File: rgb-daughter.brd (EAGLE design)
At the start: 226.1 x 74 mm, 11 parts, among them J1 INPUT

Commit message: feat(planck): add caps
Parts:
- added C10, C11, C12, C13, C15, C16, C17, C18, C19, C2, C20, C21, C22, C23, C24, C25, C26, C27, C28, C29, C3, C30, C31, C32, C33, C34, C35, C36, C37, C38, C39, C4, C40, C41, C42, C43, C44, C45, C46, C47, C48, C5, C6, C7, C8, C9: 0.1uF, SparkFun-Capacitors:0603
- added FRAME2: FRAME-LETTER, SparkFun-Aesthetics:CREATIVE_COMMONS
- added LED10, LED11, LED12, LED13, LED14, LED15, LED16, LED17, LED18, LED19, LED20, LED21, LED22, LED23, LED24, LED25, LED26, LED27, LED28, LED29, LED30, LED31, LED32, LED33, LED34, LED35, LED36, LED37, LED38, LED39, LED40, LED41, LED42, LED43, LED44, LED45, LED46, LED47, LED7, LED8, LED9: WS2812B5050, adafruit:WS2812B
- C1: value 100uF -> 0.1uF; device capacitor-wima:C2.5-3 -> SparkFun-Capacitors:0603
- J1: device SparkFun-Connectors:1X05 -> SparkFun-Connectors:1X05_1.27MM
- moved LED6 10.3 mm to (113.2, 3.17)
- moved C1 5.24 mm to (22.9, -10.2)
- moved R1 3.81 mm to (36.8, 35.6)
- moved J1 3.39 mm to (39.1, 47.2)
- moved LED3 0.99 mm to (46.5, 3.17)
- moved LED4 0.99 mm to (65.5, 3.17)
- moved LED5 0.99 mm to (84.6, 3.17)
- moved LED2 0.99 mm to (27.4, 3.17)
- moved LED1 0.13 mm to (8.37, 3.17)
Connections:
- new net DO: LED23.2-DOUT, LED25.4-DIN
- new net N$10: LED8.2-DOUT, LED9.4-DIN
- new net N$11: LED10.4-DIN, LED9.2-DOUT
- new net N$12: LED10.2-DOUT, LED11.4-DIN
- new net N$13: LED11.2-DOUT, LED12.4-DIN
- new net N$14: LED14.2-DOUT, LED15.4-DIN
- new net N$15: LED15.2-DOUT, LED16.4-DIN
- new net N$16: LED16.2-DOUT, LED17.4-DIN
- new net N$17: LED17.2-DOUT, LED18.4-DIN
- new net N$18: LED19.2-DOUT, LED20.4-DIN
- new net N$19: LED20.2-DOUT, LED21.4-DIN
- new net N$20: LED21.2-DOUT, LED22.4-DIN
- new net N$21: LED22.2-DOUT, LED23.4-DIN
- new net N$22: LED24.4-DIN, LED47.2-DOUT
- new net N$23: LED6.2-DOUT, LED7.4-DIN
- new net N$24: LED13.2-DOUT, LED14.4-DIN
- new net N$25: LED18.2-DOUT, LED19.4-DIN
- new net N$26: LED25.2-DOUT, LED26.4-DIN
- new net N$29: LED26.2-DOUT, LED27.4-DIN
- new net N$30: LED27.2-DOUT, LED28.4-DIN
- new net N$31: LED28.2-DOUT, LED29.4-DIN
- new net N$32: LED29.2-DOUT, LED30.4-DIN
- new net N$33: LED31.2-DOUT, LED32.4-DIN
- new net N$34: LED32.2-DOUT, LED33.4-DIN
- new net N$35: LED33.2-DOUT, LED34.4-DIN
- new net N$36: LED34.2-DOUT, LED35.4-DIN
- new net N$37: LED35.2-DOUT, LED36.4-DIN
- new net N$38: LED38.2-DOUT, LED39.4-DIN
- new net N$39: LED39.2-DOUT, LED40.4-DIN
- new net N$40: LED40.2-DOUT, LED41.4-DIN
- new net N$41: LED41.2-DOUT, LED42.4-DIN
- new net N$42: LED43.2-DOUT, LED44.4-DIN
- new net N$43: LED45.2-DOUT, LED46.4-DIN
- new net N$44: LED46.2-DOUT, LED47.4-DIN
- new net N$46: LED30.2-DOUT, LED31.4-DIN
- new net N$47: LED36.2-DOUT, LED37.4-DIN
- new net N$48: LED37.2-DOUT, LED38.4-DIN
- new net N$49: LED42.2-DOUT, LED43.4-DIN
- new net N$50: LED44.2-DOUT, LED45.4-DIN
- new net N$8: LED7.2-DOUT, LED8.4-DIN
- new net N$9: LED12.2-DOUT, LED13.4-DIN
- net GND: now also C10.2, C11.2, C12.2, C13.2, C15.2, C16.2, C17.2, C18.2, C19.2, C2.2, C20.2, C21.2, C22.2, C23.2, C24.2, C25.2, C26.2, C27.2, C28.2, C29.2, C3.2, C30.2, C31.2, C32.2, C33.2, C34.2, C35.2, C36.2, C37.2, C38.2, C39.2, C4.2, C40.2, C41.2, C42.2, C43.2, C44.2, C45.2, C46.2, C47.2, C48.2, C5.2, C6.2, C7.2, C8.2, C9.2, LED10.3-GND, LED11.3-GND, LED12.3-GND, LED13.3-GND, LED14.3-GND, LED15.3-GND, LED16.3-GND, LED17.3-GND, LED18.3-GND, LED19.3-GND, LED20.3-GND, LED21.3-GND, LED22.3-GND, LED23.3-GND, LED24.3-GND, LED25.3-GND, LED26.3-GND, LED27.3-GND, LED28.3-GND, LED29.3-GND, LED30.3-GND, LED31.3-GND, LED32.3-GND, LED33.3-GND, LED34.3-GND, LED35.3-GND, LED36.3-GND, LED37.3-GND, LED38.3-GND, LED39.3-GND, LED40.3-GND, LED41.3-GND, LED42.3-GND, LED43.3-GND, LED44.3-GND, LED45.3-GND, LED46.3-GND, LED47.3-GND, LED7.3-GND, LED8.3-GND, LED9.3-GND
- net VDD: now also C10.1, C11.1, C12.1, C13.1, C15.1, C16.1, C17.1, C18.1, C19.1, C2.1, C20.1, C21.1, C22.1, C23.1, C24.1, C25.1, C26.1, C27.1, C28.1, C29.1, C3.1, C30.1, C31.1, C32.1, C33.1, C34.1, C35.1, C36.1, C37.1, C38.1, C39.1, C4.1, C40.1, C41.1, C42.1, C43.1, C44.1, C45.1, C46.1, C47.1, C48.1, C5.1, C6.1, C7.1, C8.1, C9.1, LED10.1-VDD, LED11.1-VDD, LED12.1-VDD, LED13.1-VDD, LED14.1-VDD, LED15.1-VDD, LED16.1-VDD, LED17.1-VDD, LED18.1-VDD, LED19.1-VDD, LED20.1-VDD, LED21.1-VDD, LED22.1-VDD, LED23.1-VDD, LED24.1-VDD, LED25.1-VDD, LED26.1-VDD, LED27.1-VDD, LED28.1-VDD, LED29.1-VDD, LED30.1-VDD, LED31.1-VDD, LED32.1-VDD, LED33.1-VDD, LED34.1-VDD, LED35.1-VDD, LED36.1-VDD, LED37.1-VDD, LED38.1-VDD, LED39.1-VDD, LED40.1-VDD, LED41.1-VDD, LED42.1-VDD, LED43.1-VDD, LED44.1-VDD, LED45.1-VDD, LED46.1-VDD, LED47.1-VDD, LED7.1-VDD, LED8.1-VDD, LED9.1-VDD

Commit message: 🐛 rebuilding schematic with design blocks
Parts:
- added C14: 0.1uF, SparkFun-Capacitors:0603
- added LED48: WS2812B5050, adafruit:WS2812B
- moved C24 251.4 mm to (223.5, 22.9), turned to 90 degrees
- moved C12 237.6 mm to (223.5, 3.81), turned to 90 degrees
- moved C23 235.8 mm to (208.3, 22.9), turned to 90 degrees
- moved C48 233.5 mm to (223.5, 61.0), turned to 90 degrees
- moved C47 225.5 mm to (208.3, 61.0), turned to 90 degrees
- moved C11 222.3 mm to (208.3, 3.81), turned to 90 degrees
- moved C22 216.6 mm to (189.2, 22.9), turned to 90 degrees
- moved C46 214.2 mm to (189.2, 61.0), turned to 90 degrees
- moved LED36 211.2 mm to (7.62, 61.0)
- moved LED24 211.1 mm to (7.62, 41.9)
- moved LED12 209.6 mm to (217.2, 3.81)
- moved C10 203.2 mm to (189.2, 3.81), turned to 90 degrees
- moved C45 203.0 mm to (170.2, 61.0), turned to 90 degrees
- moved C36 199.5 mm to (223.5, 41.9), turned to 90 degrees
- moved C21 194.0 mm to (170.2, 22.9), turned to 90 degrees
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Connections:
- new net N$25: LED23.2-DOUT, LED48.4-DIN
- net DO: now also LED24.4-DIN, LED48.2-DOUT; no longer LED23.2-DOUT, LED25.4-DIN
- net GND: now also C14.2, LED48.3-GND
- net N$22: now also LED24.2-DOUT, LED25.4-DIN; no longer LED24.4-DIN, LED47.2-DOUT
- net VDD: now also C14.1, LED48.1-VDD

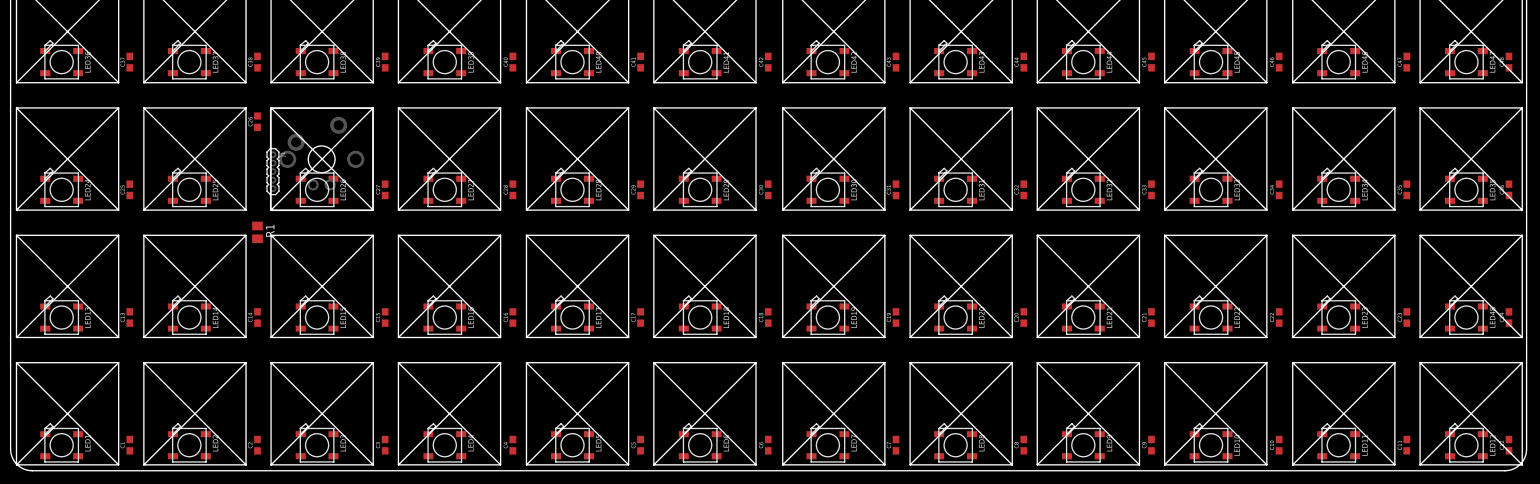
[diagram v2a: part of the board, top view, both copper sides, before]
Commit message: 🐛 moving ws2812b's under LED holes
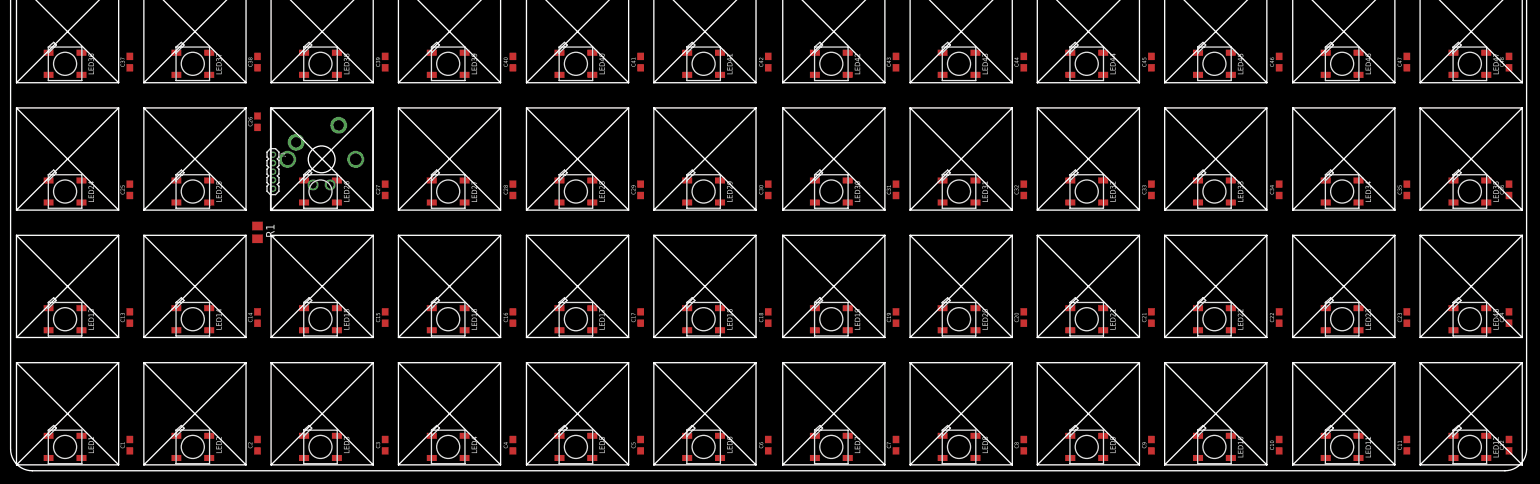
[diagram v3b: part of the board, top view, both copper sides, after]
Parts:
- moved LED10 0.57 mm to (179.6, 3.56)
- moved LED12 0.57 mm to (217.7, 3.56)
- moved LED4 0.57 mm to (65.3, 3.56)
- moved LED5 0.57 mm to (84.3, 3.56)
- moved LED8 0.57 mm to (141.5, 3.56)
- moved LED16 0.57 mm to (65.3, 22.6)
- moved LED17 0.57 mm to (84.3, 22.6)
- moved LED20 0.57 mm to (141.5, 22.6)
- moved LED22 0.57 mm to (179.6, 22.6)
- moved LED27 0.57 mm to (65.3, 41.7)
- moved LED28 0.57 mm to (84.3, 41.7)
- moved LED31 0.57 mm to (141.5, 41.7)
- moved LED33 0.57 mm to (179.6, 41.7)
- moved LED35 0.57 mm to (217.7, 41.7)
- moved LED39 0.57 mm to (65.3, 60.7)
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
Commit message: ✨ initial routing work
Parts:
- moved U$1 79.0 mm to (-23.4, 9.62)
- moved C27 1.27 mm to (55.9, 40.6)
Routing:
- net N$1: track 0.00 -> 65.9 mm
- net VDD: track 0.00 -> 31.0 mm, vias 0 -> 1
- net GND: track 0.00 -> 29.9 mm
- net N$26: track 0.00 -> 25.5 mm, vias 0 -> 2
- net N$27: track 0.00 -> 19.2 mm, vias 0 -> 2
- net N$3: track 0.00 -> 9.07 mm
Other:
- outline, holes or cut-outs redrawn

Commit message: ✨ finished routing
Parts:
- moved U$1 257.8 mm to (234.4, 8.35)
- moved C26 10.5 mm to (34.3, 41.9)
- moved C24 10.2 mm to (218.4, 31.8), turned to 180 degrees
- moved C36 10.2 mm to (218.4, 50.8), turned to 180 degrees
- moved C12 10.2 mm to (218.4, 12.7), turned to 180 degrees
- moved C48 10.2 mm to (218.4, 69.8), turned to 180 degrees
- moved R1 2.54 mm to (36.8, 33.0)
- moved C27 1.27 mm to (55.9, 41.9)
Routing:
- net GND: track 29.9 -> 1021.1 mm, vias 0 -> 4
- net VDD: track 31.0 -> 1020.6 mm, vias 1 -> 2
- net N$36: track 0.00 -> 225.1 mm
- net N$13: track 0.00 -> 225.1 mm
- net DO: track 0.00 -> 225.1 mm
- net N$47: track 0.00 -> 15.5 mm
- net N$40: track 0.00 -> 15.5 mm
- net N$39: track 0.00 -> 15.5 mm
- net N$25: track 0.00 -> 15.5 mm
- net N$12: track 0.00 -> 15.5 mm
- net N$35: track 0.00 -> 15.5 mm
- net N$6: track 0.00 -> 15.5 mm
- net N$5: track 0.00 -> 15.5 mm
- net N$46: track 0.00 -> 15.5 mm
- net N$44: track 0.00 -> 15.5 mm
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
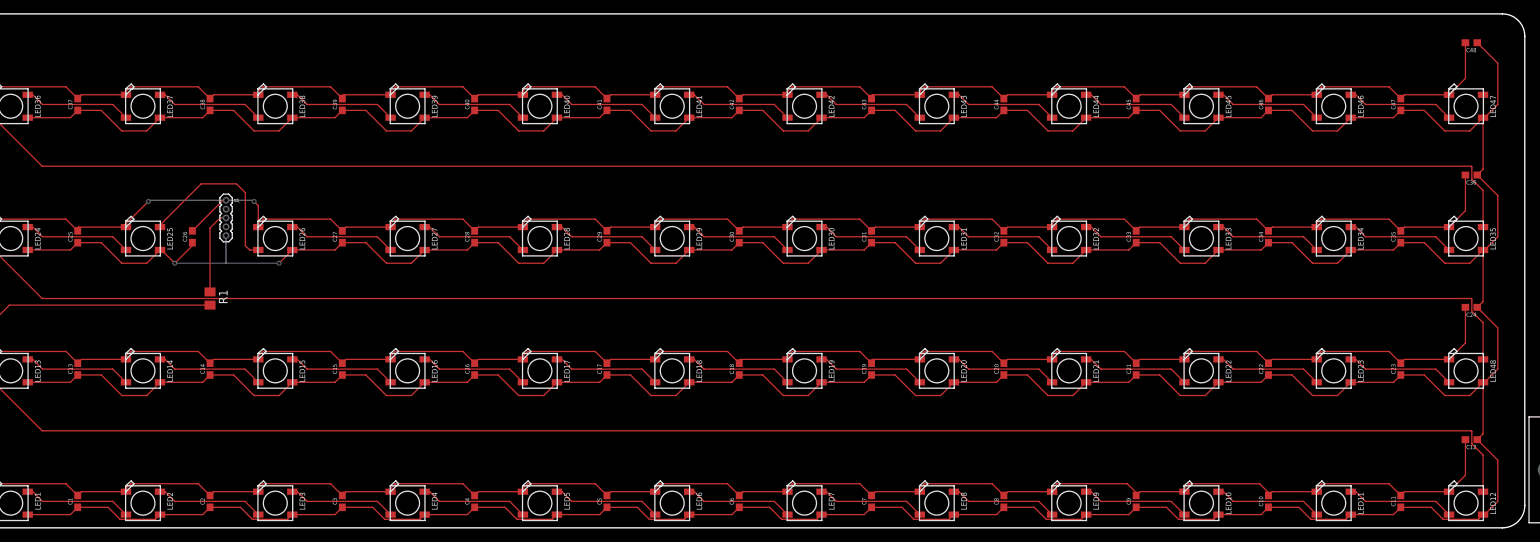
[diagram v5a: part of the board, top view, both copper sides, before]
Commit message: 🐛 moving caps to avoid contact with switches
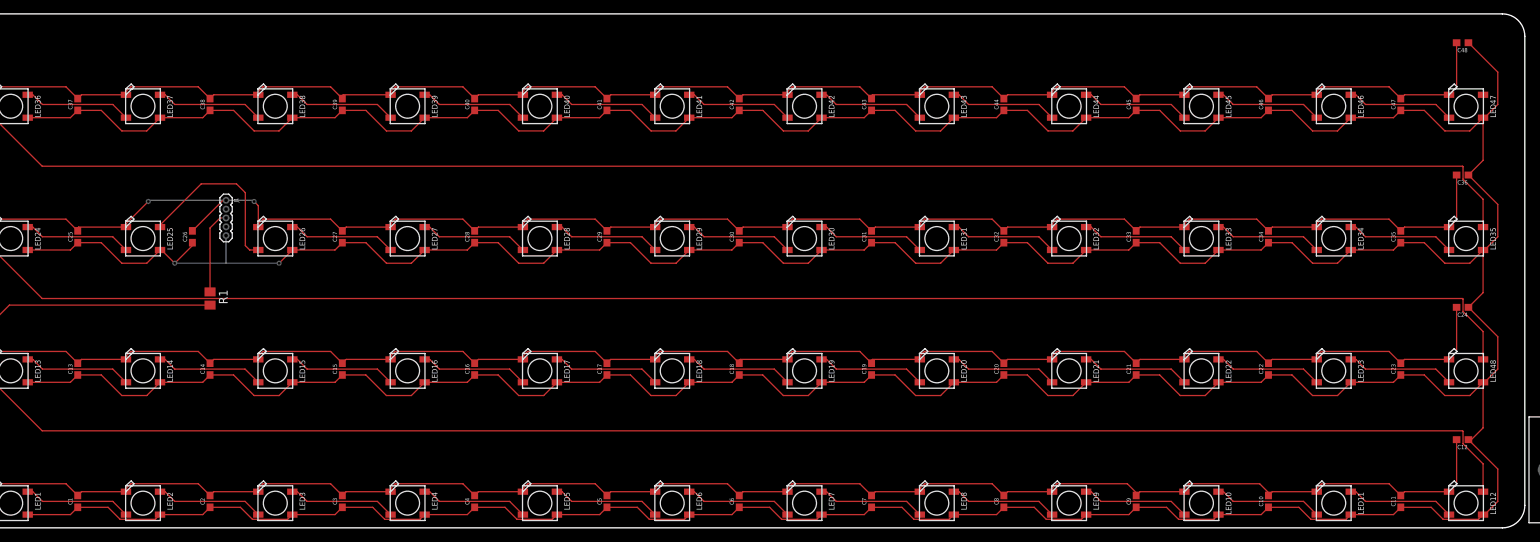
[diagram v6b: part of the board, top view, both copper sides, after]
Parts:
- moved C12 1.27 mm to (217.2, 12.7)
- moved C24 1.27 mm to (217.2, 31.8)
- moved C36 1.27 mm to (217.2, 50.8)
- moved C48 1.27 mm to (217.2, 69.8)
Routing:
- net VDD: track 1020.6 -> 1024.4 mm
- net GND: track 1021.1 -> 1019.0 mm
- net N$13: track 225.1 -> 224.4 mm
- net N$36: track 225.1 -> 224.4 mm
- net DO: track 225.1 -> 224.4 mm

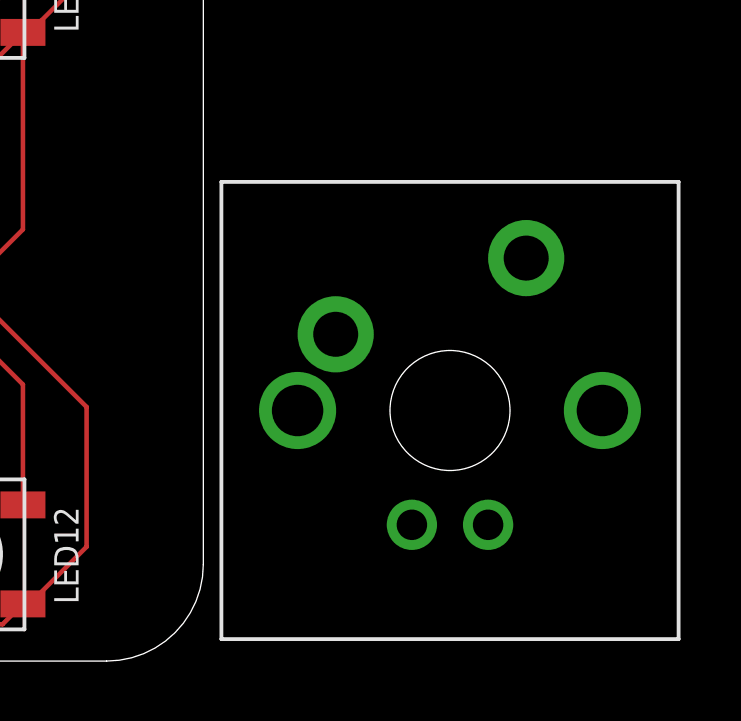
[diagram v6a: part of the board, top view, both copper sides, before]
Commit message: 🔥 removing test cherry switch
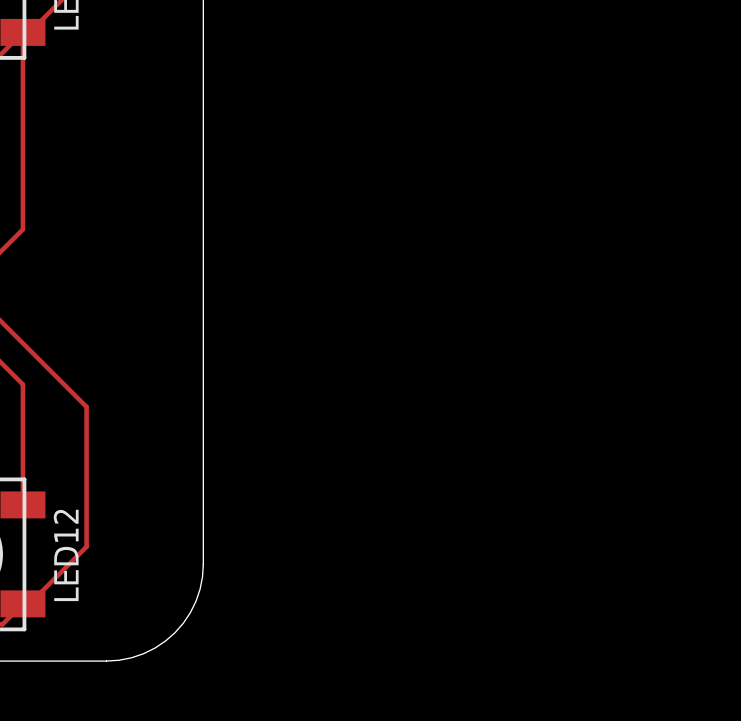
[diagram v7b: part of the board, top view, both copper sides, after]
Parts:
- removed U$1: CHERRY-MX-LED, cherrymx:CHERRY-MX-LED
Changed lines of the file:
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@@
 <element name="J1" library="SparkFun-Connectors" library_urn="urn:adsk.eagle:library:513" package="1X05_1.27MM" package3d_urn="urn:adsk.eagle:package:38110/1" value="INPUT" x="39.1395625" y="47.159578125" rot="R270"/>
 <element name="R1" library="resistor" library_urn="urn:adsk.eagle:library:348" package="M0805" package3d_urn="urn:adsk.eagle:package:26079/1" value="100" x="36.83" y="33.02" rot="R270"/>
-<element name="U$1" library="cherrymx" package="CHERRY-MX-LED" value="CHERRY-MX-LED" x="234.3633125" y="8.352565625"/>
 <element name="FRAME2" library="SparkFun-Aesthetics" library_urn="urn:adsk.eagle:library:507" package="CREATIVE_COMMONS" package3d_urn="urn:adsk.eagle:package:37121/1" value="FRAME-LETTER" x="157.48" y="-19.05"/>
 <element name="LED1" library="adafruit" library_urn="urn:adsk.eagle:library:420" package="WS2812B" value="WS2812B5050" x="8.128" y="3.556"/>

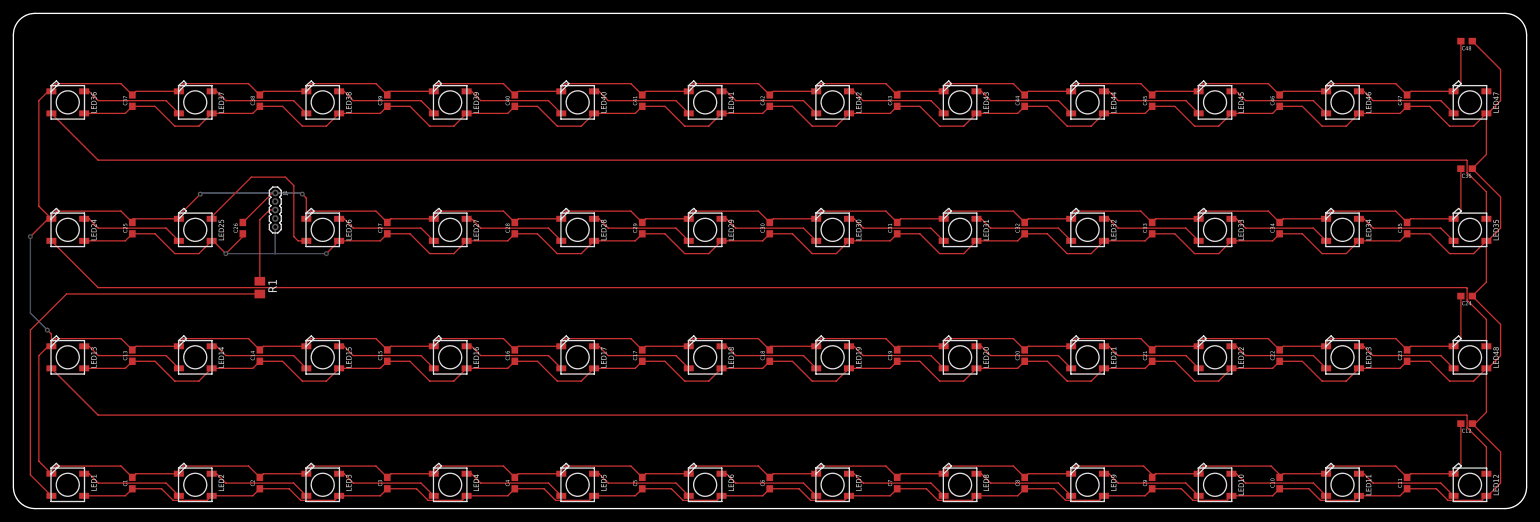
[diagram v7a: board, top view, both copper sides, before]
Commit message: 🐛 resizing and moving traces
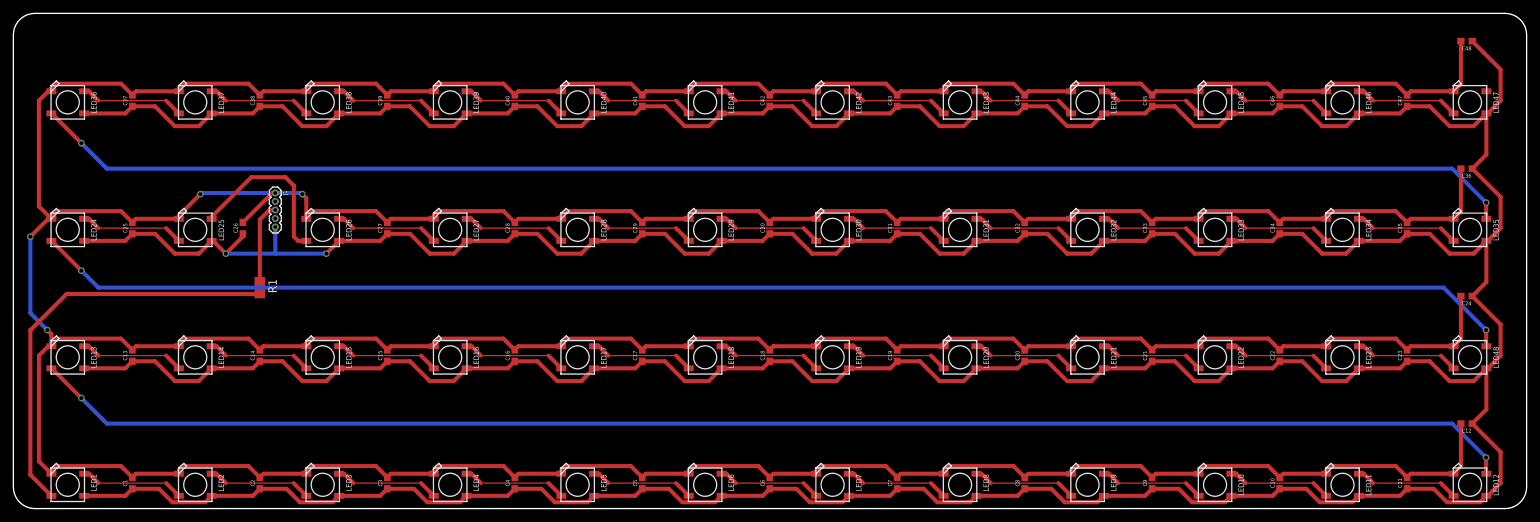
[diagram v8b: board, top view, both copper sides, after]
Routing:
- net N$36: track 224.4 -> 222.4 mm, vias 0 -> 2
- net N$13: track 224.4 -> 222.4 mm, vias 0 -> 2
- net DO: track 224.4 -> 222.4 mm, vias 0 -> 2
- net VDD: track 1024.4 -> 1026.2 mm
- net GND: track 1019.0 -> 1017.7 mm
